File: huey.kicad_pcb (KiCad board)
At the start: 2 copper layers, 50 x 50 mm, 22 parts, among them CON1 BARREL_JACK, P1 TO_LEDS, P2 NPTC161KFXC-RC, P3 NPTC121KFXC-RC, P4 CONN_01X06, P5 CONN_01X02, P6 CONN_01X02, Q1 MF-DSC-SOT233-BSS138, U1 FEATHER_M0_WIFI

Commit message: Some additions to the main board layout, and a new design of the top board.
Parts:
- added P7: CONN_01X02, Pin_Headers:Pin_Header_Straight_1x02, F.Cu at (59.7, 64.8)
- P1: footprint Pin_Headers:Pin_Header_Straight_1x03 -> Huey:LED_BOARD_CONNECTOR
- moved FID3 7.81 mm to (65.0, 59.0)
- moved P5 3.17 mm to (59.7, 90.2)
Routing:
- net Net-(P2-Pad1): track 0.00 -> 7.15 mm
- net Net-(P2-Pad15): track 6.88 -> 10.1 mm
- net Net-(P2-Pad14): track 4.18 -> 6.24 mm
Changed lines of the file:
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@@
 (kicad_pcb (version 4) (host pcbnew 4.0.5+dfsg1-4)
   (general
-    (links 37)
+    (links 39)
     (no_connects 0)
-    (area 52.728572 48.8 116.5 110.342021)
+    (area 52.728572 48.8 116.5 114.700001)
     (thickness 1.6)
-    (drawings 12)
-    (tracks 102)
+    (drawings 13)
+    (tracks 105)
     (zones 0)
-    (modules 22)
+    (modules 23)
     (nets 37)
   )
@@
     (visible_elements FFFFFF7F)
     (pcbplotparams
-      (layerselection 0x00030_80000001)
-      (usegerberextensions false)
+      (layerselection 0x010fc_80000001)
+      (usegerberextensions true)
       (excludeedgelayer true)
       (linewidth 0.100000)
@@
       (padsonsilk false)
       (subtractmaskfromsilk false)
-      (outputformat 4)
+      (outputformat 1)
       (mirror false)
       (drillshape 0)
       (scaleselection 1)
-      (outputdirectory ""))
+      (outputdirectory gerber))
   )
   (net 0 "")
@@
   )
   (module Pin_Headers:Pin_Header_Straight_1x02 (layer F.Cu)
+    (at 59.69 64.77)
+    (descr "Through hole pin header")
+    (tags "pin header")
+    (fp_text reference P7 (at 0 -5.1) (layer F.SilkS) hide
+      (effects (font (size 1 1) (thickness 0.15)))
+    )
+    (fp_text value CONN_01X02 (at 0 -3.1) (layer F.Fab) hide
+      (effects (font (size 1 1) (thickness 0.15)))
+    )
+    (fp_text user GND (at -3.175 2.54) (layer F.SilkS)
+      (effects (font (size 1 1) (thickness 0.15)))
+    )
+    (fp_text user RST (at -3.175 0) (layer F.SilkS)
+      (effects (font (size 1 1) (thickness 0.15)))
+    )
+    (fp_line (start 1.27 1.27) (end 1.27 3.81) (layer F.SilkS) (width 0.15))
+    (fp_line (start 1.55 -1.55) (end 1.55 0) (layer F.SilkS) (width 0.15))
+    (fp_line (start -1.75 -1.75) (end -1.75 4.3) (layer F.CrtYd) (width 0.05))
+    (fp_line (start 1.75 -1.75) (end 1.75 4.3) (layer F.CrtYd) (width 0.05))
+    (fp_line (start -1.75 -1.75) (end 1.75 -1.75) (layer F.CrtYd) (width 0.05))
+    (fp_line (start -1.75 4.3) (end 1.75 4.3) (layer F.CrtYd) (width 0.05))
+    (fp_line (start 1.27 1.27) (end -1.27 1.27) (layer F.SilkS) (width 0.15))
+    (fp_line (start -1.55 0) (end -1.55 -1.55) (layer F.SilkS) (width 0.15))
+    (fp_line (start -1.55 -1.55) (end 1.55 -1.55) (layer F.SilkS) (width 0.15))
+    (fp_line (start -1.27 1.27) (end -1.27 3.81) (layer F.SilkS) (width 0.15))
+    (fp_line (start -1.27 3.81) (end 1.27 3.81) (layer F.SilkS) (width 0.15))
+    (pad 1 thru_hole rect (at 0 0) (size 2.032 2.032) (drill 1.016) (layers *.Cu *.Mask)
+      (net 12 "Net-(P2-Pad1)"))
+    (pad 2 thru_hole oval (at 0 2.54) (size 2.032 2.032) (drill 1.016) (layers *.Cu *.Mask)
+      (net 3 GND))
+    (model Pin_Headers.3dshapes/Pin_Header_Straight_1x02.wrl
+      (at (xyz 0 -0.05 0))
+      (scale (xyz 1 1 1))
+      (rotate (xyz 0 0 90))
+    )
+  )
+  (module Pin_Headers:Pin_Header_Straight_1x02 (layer F.Cu)
     (at 88.9 97.79)
     (descr "Through hole pin header")
@@
   )
   (module Pin_Headers:Pin_Header_Straight_1x02 (layer F.Cu)
-    (at 59.69 93.345)
+    (at 59.69 90.17)
     (descr "Through hole pin header")
     (tags "pin header")
@@
       (net 10 "Net-(SD1-Pad10)"))
   )
-  (module Pin_Headers:Pin_Header_Straight_1x03 (layer F.Cu)
-    (at 78.74 65.405 270)
-    (descr "Through hole pin header")
-    (tags "pin header")
-    (fp_text reference P1 (at 3.175 -0.635 270) (layer F.SilkS) hide
-      (effects (font (size 1 1) (thickness 0.15)))
-    )
-    (fp_text value TO_LEDS (at -3 4 360) (layer F.SilkS)
-      (effects (font (size 1.016 1.016) (thickness 0.254)))
-    )
-    (fp_text user DATA (at 3.81 3.81 270) (layer F.SilkS)
-      (effects (font (size 1.016 1.016) (thickness 0.254)))
-    )
-    (fp_text user GND (at 3.81 7.62 270) (layer F.SilkS)
-      (effects (font (size 1.016 1.016) (thickness 0.254)))
-    )
-    (fp_text user +5V (at 3.81 0 270) (layer F.SilkS)
-      (effects (font (size 1.016 1.016) (thickness 0.254)))
-    )
-    (pad 1 thru_hole circle (at 0 0 270) (size 3.556 3.556) (drill 2.032) (layers *.Cu *.Mask)
-      (net 1 +5V))
-    (pad 2 thru_hole oval (at 0 3.81 270) (size 2.032 1.7272) (drill 1.016) (layers *.Cu *.Mask)
-      (net 2 "Net-(P1-Pad2)"))
-    (pad 3 thru_hole circle (at 0 7.62 270) (size 3.556 3.556) (drill 2.032) (layers *.Cu *.Mask)
-      (net 3 GND))
-    (model Pin_Headers.3dshapes/Pin_Header_Straight_1x03.wrl
-      (at (xyz 0 -0.1 0))
-      (scale (xyz 1 1 1))
-      (rotate (xyz 0 0 90))
-    )
-  )
   (module Huey:MF_Discrete_Semiconductor-SOT-23-3 (layer F.Cu)
     (at 75.25 76.45 90)
@@
   )
   (module Fiducials:Fiducial_1mm_Dia_2.54mm_Outer_CopperTop (layer F.Cu)
-    (at 59 64)
+    (at 65 59)
     (descr "Circular Fiducial, 1mm bare copper top; 2.54mm keepout")
     (tags marker)
@@
     (fp_line (start 11.43 25.4) (end -11.43 25.4) (layer F.SilkS) (width 0.15))
     (fp_line (start -11.43 25.4) (end -11.43 -25.4) (layer F.SilkS) (width 0.15))
+  )
+  (module Huey:LED_BOARD_CONNECTOR (layer F.Cu)
+    (at 78.74 65.405 270)
+    (descr "Through hole pin header")
+    (tags "pin header")
+    (fp_text reference P1 (at 3.175 -0.635 270) (layer F.SilkS) hide
+      (effects (font (size 1 1) (thickness 0.15)))
+    )
+    (fp_text value TO_LEDS (at -3 4 360) (layer F.SilkS)
+      (effects (font (size 1.016 1.016) (thickness 0.254)))
+    )
+    (fp_text user DATA (at 3.81 3.81 270) (layer F.SilkS)
+      (effects (font (size 1.016 1.016) (thickness 0.254)))
+    )
+    (fp_text user GND (at 3.81 7.62 270) (layer F.SilkS)
+      (effects (font (size 1.016 1.016) (thickness 0.254)))
+    )
+    (fp_text user +5V (at 3.81 0 270) (layer F.SilkS)
+      (effects (font (size 1.016 1.016) (thickness 0.254)))
+    )
+    (pad 1 thru_hole circle (at 0 0 270) (size 3.556 3.556) (drill 2.032) (layers *.Cu *.Mask)
+      (net 1 +5V))
+    (pad 2 thru_hole oval (at 0 3.81 270) (size 2.032 1.7272) (drill 1.016) (layers *.Cu *.Mask)
+      (net 2 "Net-(P1-Pad2)"))
+    (pad 3 thru_hole circle (at 0 7.62 270) (size 3.556 3.556) (drill 2.032) (layers *.Cu *.Mask)
+      (net 3 GND))
+    (model Pin_Headers.3dshapes/Pin_Header_Straight_1x03.wrl
+      (at (xyz 0 -0.1 0))
+      (scale (xyz 1 1 1))
+      (rotate (xyz 0 0 90))
+    )
+  )
+  (dimension 42 (width 0.3) (layer Cmts.User)
+    (gr_text "42.000 mm" (at 80 113.35) (layer Cmts.User)
+      (effects (font (size 1.5 1.5) (thickness 0.3)))
+    )
+    (feature1 (pts (xy 101 101) (xy 101 114.7)))
+    (feature2 (pts (xy 59 101) (xy 59 114.7)))
+    (crossbar (pts (xy 59 112) (xy 101 112)))
+    (arrow1a (pts (xy 101 112) (xy 99.873496 112.586421)))
+    (arrow1b (pts (xy 101 112) (xy 99.873496 111.413579)))
+    (arrow2a (pts (xy 59 112) (xy 60.126504 112.586421)))
+    (arrow2b (pts (xy 59 112) (xy 60.126504 111.413579)))
   )
   (dimension 50 (width 0.3) (layer Cmts.User)
@@
   (via (at 71.755 90.17) (size 0.6) (drill 0.4) (layers F.Cu B.Cu) (net 10))
   (segment (start 71.59244 90.00744) (end 71.755 90.17) (width 0.25) (layer F.Cu) (net 10))
+  (segment (start 65.785 62.23) (end 62.23 62.23) (width 0.25) (layer F.Cu) (net 12))
+  (segment (start 62.23 62.23) (end 59.69 64.77) (width 0.25) (layer F.Cu) (net 12))
   (segment (start 59.69 72.39) (end 65.785 72.39) (width 0.25) (layer F.Cu) (net 14))
   (segment (start 62.485 74.93) (end 59.69 74.93) (width 0.25) (layer F.Cu) (net 15))
@@
   (segment (start 69.215 92.71) (end 69.85 93.345) (width 0.25) (layer F.Cu) (net 22))
   (segment (start 64.84 92.7) (end 66.05 92.7) (width 0.25) (layer F.Cu) (net 22))
-  (segment (start 59.69 93.345) (end 61.595 93.345) (width 0.25) (layer F.Cu) (net 23))
-  (segment (start 62.485 94.235) (end 62.485 95.25) (width 0.25) (layer F.Cu) (net 23))
-  (segment (start 61.595 93.345) (end 62.485 94.235) (width 0.25) (layer F.Cu) (net 23))
-  (segment (start 65.785 97.79) (end 61.595 97.79) (width 0.25) (layer F.Cu) (net 24))
-  (segment (start 61.595 97.79) (end 59.69 95.885) (width 0.25) (layer F.Cu) (net 24))
+  (segment (start 59.69 90.17) (end 62.23 92.71) (width 0.25) (layer F.Cu) (net 23))
+  (segment (start 62.23 92.71) (end 62.23 94.995) (width 0.25) (layer F.Cu) (net 23))
+  (segment (start 62.23 94.995) (end 62.485 95.25) (width 0.25) (layer F.Cu) (net 23))
+  (segment (start 59.69 92.71) (end 59.69 95.885) (width 0.25) (layer F.Cu) (net 24))
+  (segment (start 61.595 97.79) (end 65.785 97.79) (width 0.25) (layer F.Cu) (net 24))
+  (segment (start 59.69 95.885) (end 61.595 97.79) (width 0.25) (layer F.Cu) (net 24))
   (segment (start 75.7682 100.10394) (end 75.7682 98.8568) (width 0.25) (layer F.Cu) (net 31))
   (segment (start 78.105 87.63) (end 86.105 87.63) (width 0.25) (layer F.Cu) (net 31))

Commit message: updating jack component
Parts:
- CON1: value BARREL_JACK -> PJ-036AH-SMT-TR
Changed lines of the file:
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@@
     (links 39)
     (no_connects 0)
-    (area 52.728572 48.8 116.5 114.700001)
+    (area 54.924999 54.924999 105.075001 105.075001)
     (thickness 1.6)
     (drawings 13)
@@
       (effects (font (size 1 1) (thickness 0.15)))
     )
-    (fp_text value BARREL_JACK (at -1.5 0 180) (layer F.SilkS) hide
-      (effects (font (size 1 1) (thickness 0.15)))
-    )
+    (fp_text value PJ-036AH-SMT-TR (at -1.5 0 180) (layer F.SilkS) hide
+      (effects (font (size 1 1) (thickness 0.15)))
+    )

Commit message: Pushing final changes for rev 1.0
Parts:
- added P8: NPTC081KFXC-RC, Huey:FEMALE_HEADER_8x1_SMD, F.Cu at (64.1, 91.4)
- P2: value NPTC161KFXC-RC -> NPTC081KFXC-RC; footprint Huey:FEMALE_HEADER_16x1_SMD -> Huey:FEMALE_HEADER_8x1_SMD
- moved P2 6.35 mm to (64.1, 71.1)
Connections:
- P4 pad 5: Net-(P2-Pad9) -> Net-(P4-Pad5)
- P4 pad 6: Net-(P2-Pad10) -> Net-(P4-Pad6)
- P5 pad 1: Net-(P2-Pad14) -> Net-(P5-Pad1)
- P5 pad 2: Net-(P2-Pad15) -> Net-(P5-Pad2)
- SD1 pad 3: Net-(P2-Pad12) -> Net-(P8-Pad4)
- SD1 pad 5: Net-(P2-Pad11) -> Net-(P8-Pad3)
- SD1 pad 7: Net-(P2-Pad13) -> Net-(P8-Pad5)
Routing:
- net Net-(P8-Pad4): track 0.00 -> 21.0 mm, vias 0 -> 2
- net Net-(P2-Pad12): track 21.0 -> 0.00 mm, vias 2 -> 0
- net Net-(P8-Pad3): track 0.00 -> 17.8 mm
- net Net-(P2-Pad11): track 17.8 -> 0.00 mm
- net Net-(P8-Pad5): track 0.00 -> 12.7 mm
- net Net-(P2-Pad13): track 12.7 -> 0.00 mm
- net Net-(P5-Pad2): track 0.00 -> 10.1 mm
- net Net-(P2-Pad15): track 10.1 -> 0.00 mm
- net Net-(P5-Pad1): track 0.00 -> 6.24 mm
- net Net-(P2-Pad14): track 6.24 -> 0.00 mm
- net Net-(P4-Pad5): track 0.00 -> 6.09 mm
- net Net-(P2-Pad9): track 6.09 -> 0.00 mm
- net Net-(P4-Pad6): track 0.00 -> 2.80 mm
- net Net-(P2-Pad10): track 2.80 -> 0.00 mm

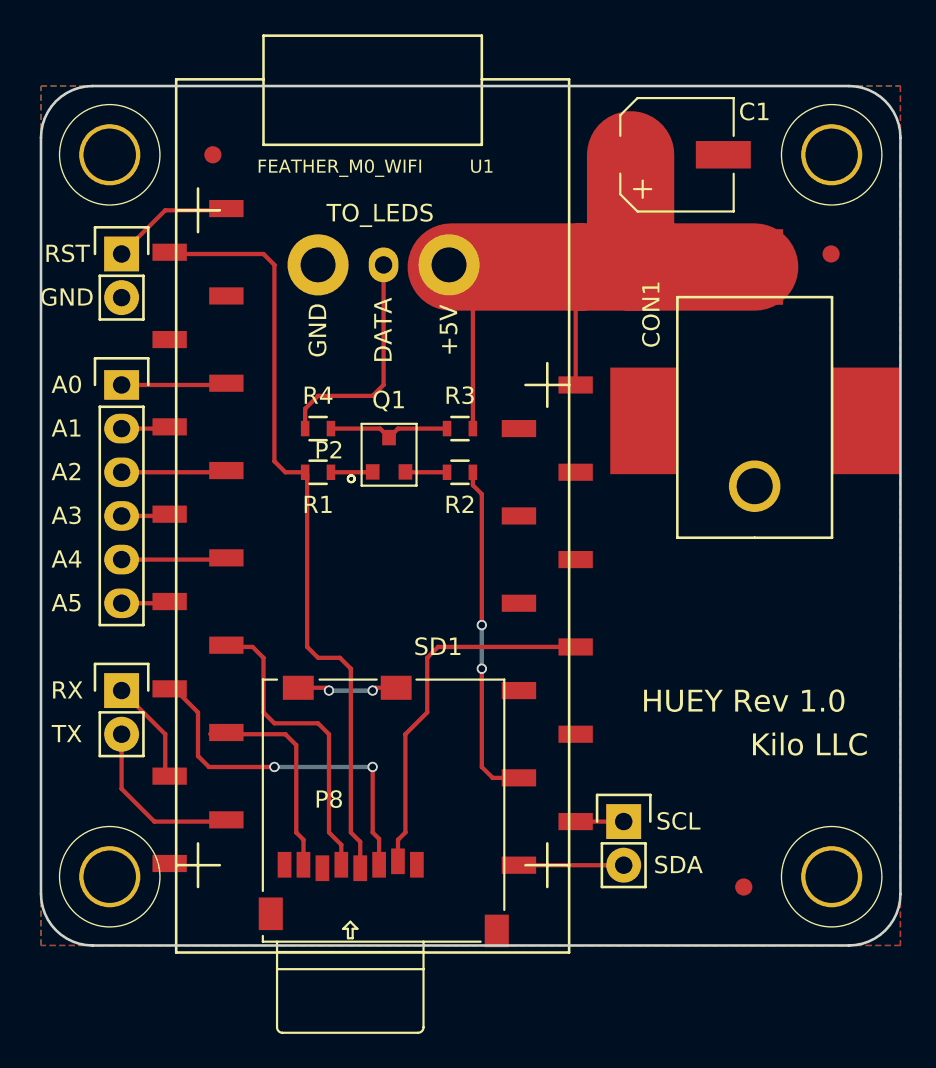
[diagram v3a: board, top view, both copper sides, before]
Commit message: Revision 1.1
Changelog:
-Re-exported copper pours to correct issues in rev 1.0
-Moved SD card to bottom for increased space
-Increased the clearance of copper pours for easier visual verification
-Added some vias to GND underneath the power jack to compensate for reduced GND plane area after increasing clearance
-Added test points for SD card data access
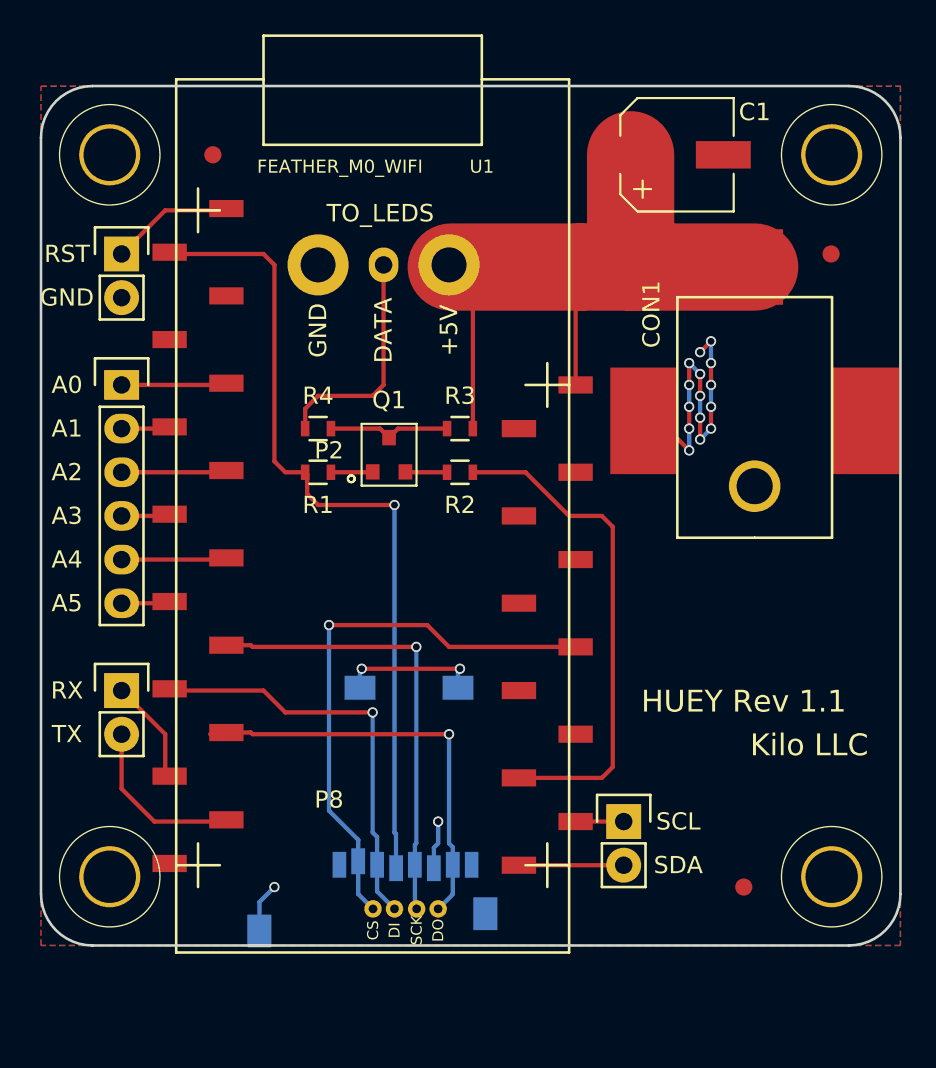
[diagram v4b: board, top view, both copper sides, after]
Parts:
- added P10: CONN_01X02, Pin_Headers:Pin_Header_Straight_1x02, F.Cu at (75.6, 102.9)
- added P9: CONN_01X02, Pin_Headers:Pin_Header_Straight_1x02, F.Cu at (78.1, 102.9)
- SD1: moved to B.Cu
- moved SD1 0.64 mm to (74.3, 97.2), turned to 0 degrees
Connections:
- net Net-(P3-Pad7) renamed /CS
- net Net-(P8-Pad3) renamed /SCLK
- net Net-(P8-Pad4) renamed /DI
- net Net-(P8-Pad5) renamed /DO
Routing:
- net GND: track 0.00 -> 25.8 mm, vias 0 -> 17
- net /DO: track 12.7 -> 24.8 mm, vias 0 -> 1
- net /CS: track 21.4 -> 32.4 mm, vias 0 -> 1
- net Net-(P3-Pad10): track 19.8 -> 29.1 mm, vias 2 -> 0
- net /SCLK: track 17.8 -> 26.4 mm, vias 0 -> 1
- net /DI: track 21.0 -> 24.7 mm, vias 2 -> 1
- net +3V3: track 44.9 -> 47.8 mm, vias 0 -> 1
- net Net-(SD1-Pad10): track 5.83 -> 8.02 mm
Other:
- board text added: "HUEY Rev 1.1"
- board text removed: "HUEY Rev 1.0"

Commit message: Revision 1.1
Changelog:
	- Removed R2 resistor from the logic level converter
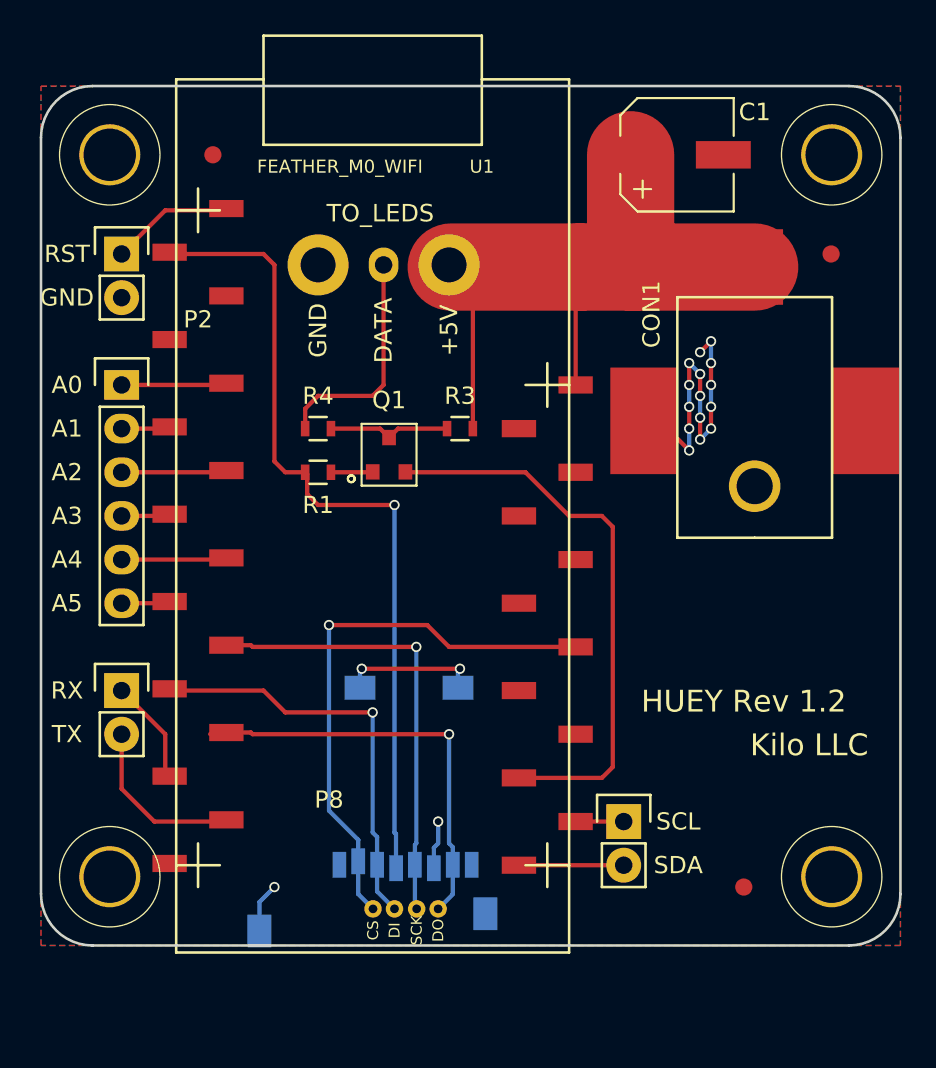
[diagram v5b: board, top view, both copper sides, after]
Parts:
- removed R2: MF-RES-0603-1K, Resistors_SMD:R_0603
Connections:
- Q1 pad 2: Net-(Q1-Pad2) -> Net-(P3-Pad10)
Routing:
- net Net-(P3-Pad10): track 29.1 -> 33.1 mm
- net Net-(Q1-Pad2): track 2.43 -> 0.00 mm
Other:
- board text added: "HUEY Rev 1.2"
- board text removed: "HUEY Rev 1.1"

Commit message: Changing 12x1 SMD header to 8x1 and 4x1 headers, for (hopefully) better part availability
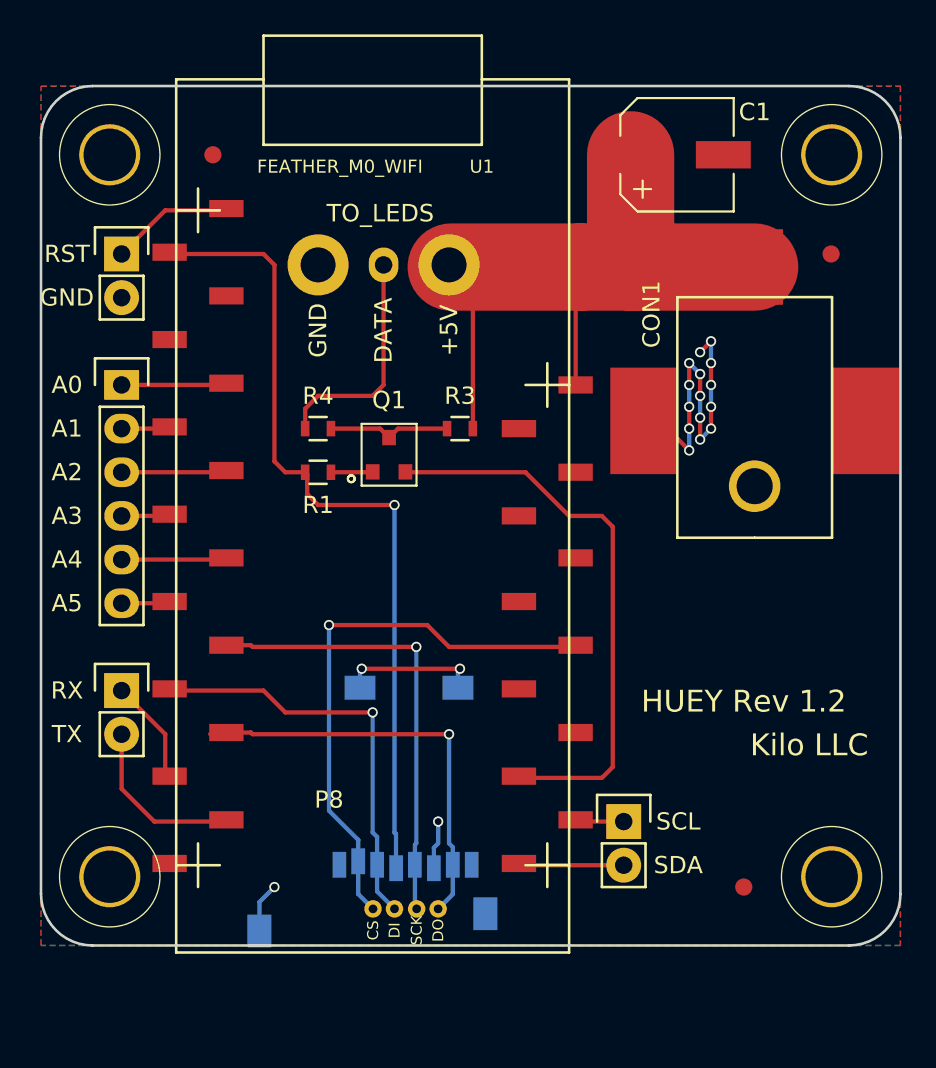
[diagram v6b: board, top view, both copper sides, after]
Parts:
- added P11: NPTC041KFXC-RC, Huey:FEMALE_HEADER_04x1_SMD, F.Cu at (84.5, 76.2)
- P3: value NPTC121KFXC-RC -> NPTC081KFXC-RC; footprint Huey:FEMALE_HEADER_12x1_SMD -> Huey:FEMALE_HEADER_8x1_SMD
- moved P3 3.81 mm to (84.5, 91.4)
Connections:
- P3 pad 1: +5V -> Net-(P3-Pad1)
- P3 pad 3: Net-(P3-Pad3) -> /CS
- P3 pad 7: /CS -> Net-(P3-Pad7)
- P6 pad 1: Net-(P3-Pad11) -> Net-(P3-Pad7)
- P6 pad 2: Net-(P3-Pad12) -> Net-(P3-Pad8)
- Q1 pad 2: Net-(P3-Pad10) -> Net-(P3-Pad6)
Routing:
- net Net-(P3-Pad6): track 0.00 -> 33.1 mm
- net Net-(P3-Pad10): track 33.1 -> 0.00 mm
- net Net-(P3-Pad8): track 0.00 -> 6.09 mm
- net Net-(P3-Pad12): track 6.09 -> 0.00 mm
- net Net-(P3-Pad7): track 0.00 -> 2.80 mm
- net Net-(P3-Pad11): track 2.80 -> 0.00 mm
